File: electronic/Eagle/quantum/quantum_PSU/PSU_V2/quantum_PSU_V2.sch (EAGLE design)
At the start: 30 parts, among them J1 90814-0204, J2 90814-0204, J3 PF0030_PC, U1 7815, U2 7812, U4 7805, U5 LD1117AV33

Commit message: PSU_V2 progress...
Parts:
- C1, C3: value (none) -> 4700 uF/25 V
- C10, C12, C4, C5, C6: value (none) -> 100 nF
- C11, C13, C7, C8, C9: value (none) -> 100 uF/25V; device passive components:CAPACITOR_5MM -> passive components:CAPACITOR_ELECTROLYTIC_8MM-THT
- C2: value (none) -> 4700 uF/25V
- U3: value (none) -> 7915
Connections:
- net +12V_OUT: now also C9.+, J2.2; no longer C9.1
- net +15V_OUT: now also C7.+, J1.1; no longer C7.1
- net +3V3_OUT: now also C13.+, J2.1; no longer C13.1
- net +5V_OUT: now also C11.+, J2.4; no longer C11.1
- net -15V_OUT: now also C8.-, J1.2; no longer C8.2
- net AGND: now also C7.-, C8.+, J1.3, J1.4; no longer C7.2, C8.1
- net DGND: now also C11.-, C13.-, C9.-, J2.3; no longer C11.2, C13.2, C9.2
- net N$1: now also TRANSFORMATOR2.P$6; no longer TRANSFORMATOR2.P$5
- net N$3: now also TRANSFORMATOR2.P$5; no longer TRANSFORMATOR2.P$6
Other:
- note added: "Output Connectors"
- moved on the sheet: C1, C10, C12, C2, C3, C4, C5, C6, D1, D2, D3, D4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

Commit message: progress PSU_V2
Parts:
- added BR3: BRIDGE_RECTIFIER, passive components:BRIDGE_RECTIFIER
- added C14, C15, C16, C17, C18: 100 nF, passive components:CAPACITOR_5MM
- added X1: (no value), electro_mechanical:CONNECTOR_3POL
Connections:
- removed net N$1: BR2.~_1, TRANSFORMATOR2.P$6, TRANSFORMATOR2.P$7
- removed net N$13: BR1.~_2, TRANSFORMATOR1.P$5
- new net N$4: TRANSFORMATOR1.P$1, TRANSFORMATOR1.P$4
- new net N$5: TRANSFORMATOR2.P$1, TRANSFORMATOR2.P$4
- new net N$6: TRANSFORMATOR2.P$8
- net +12V_OUT: now also C14.1
- net +15V_OUT: now also C18.1
- net +3V3_OUT: now also C16.1
- net +5V_OUT: now also C15.1
- net -15V_OUT: now also C17.2
- net AGND: now also C17.1, C18.2, TRANSFORMATOR1.P$5; no longer TRANSFORMATOR1.P$6
- net CHASSIS: now also X1-3.KL
- net DGND: now also BR3.-, C14.2, C15.2, C16.2
- net N$10: now also BR3.~_1, TRANSFORMATOR2.P$5; no longer TRANSFORMATOR2.P$2, TRANSFORMATOR2.P$4
- net N$2: now also BR3.+
- net N$3: now also BR1.~_2, TRANSFORMATOR1.P$6; no longer BR2.~_2, TRANSFORMATOR2.P$5, TRANSFORMATOR2.P$8
- net N$7: now also BR3.~_2, TRANSFORMATOR2.P$6; no longer TRANSFORMATOR1.P$2, TRANSFORMATOR1.P$4
- net N$8: now also X1-2.KL
- net N$9: now also TRANSFORMATOR1.P$2, TRANSFORMATOR2.P$2, X1-1.KL; no longer TRANSFORMATOR1.P$1, TRANSFORMATOR2.P$1
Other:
- moved on the sheet: BR1, BR2, C1, C10, C11, C12, C13, C2, C3, C4, C5, C6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

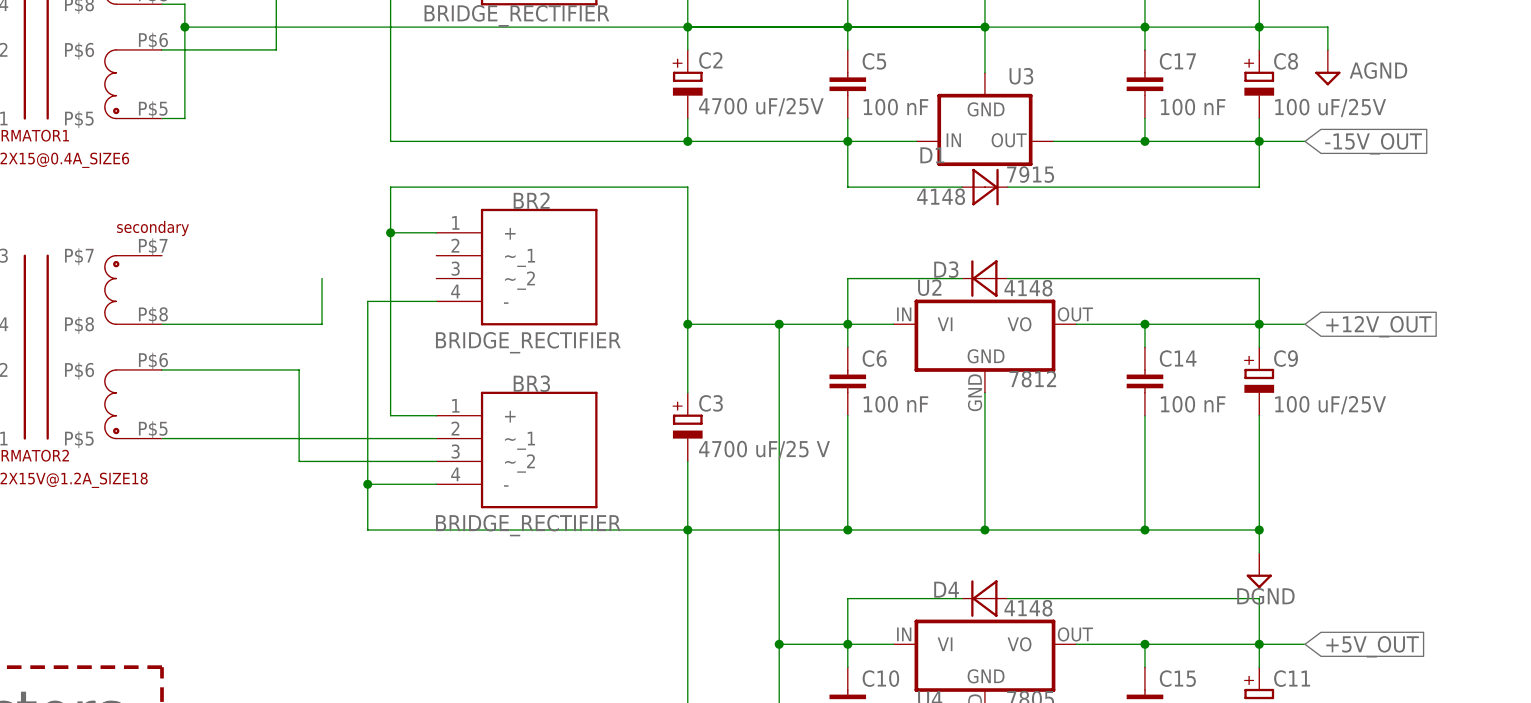
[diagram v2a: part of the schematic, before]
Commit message: created DiscoveryConnector_V1_0; Finished PSU_V2_0; Changed Light Settings in Encoder
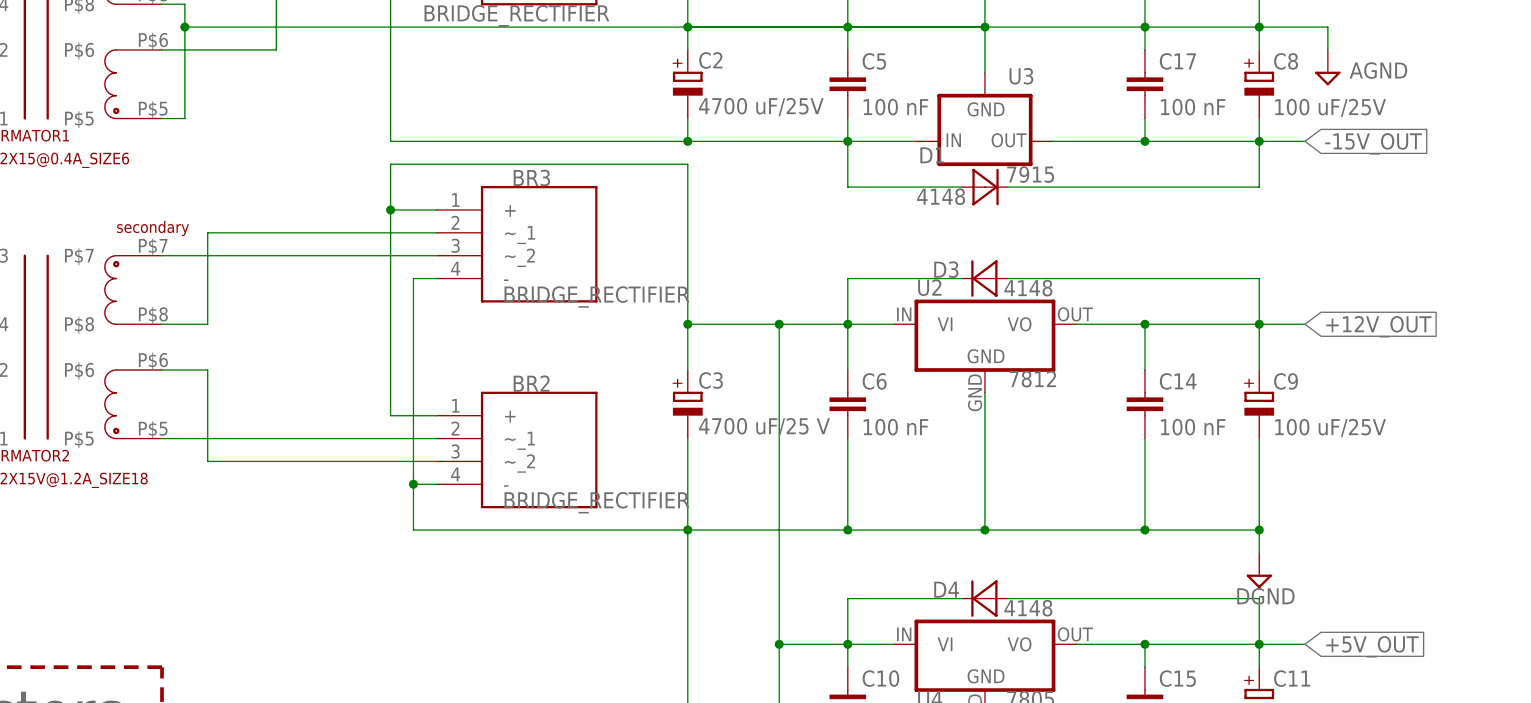
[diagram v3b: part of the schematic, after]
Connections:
- removed net N$10: BR3.~_1, TRANSFORMATOR2.P$5
- new net N$1: BR3.~_2, TRANSFORMATOR2.P$7
- new net N$12: BR2.~_1, TRANSFORMATOR2.P$5
- net N$6: now also BR3.~_1
- net N$7: now also BR2.~_2; no longer BR3.~_2
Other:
- moved on the sheet: BR2, BR3, C14, C3, C6, C9
